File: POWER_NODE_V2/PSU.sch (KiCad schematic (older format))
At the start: 0 parts

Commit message: Schematic for Power Node V2 mostly done - mostly need connectors
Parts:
- added C? (x2): 1uF / 50V / 10% / SMD 0805, symbol C
- added C? (x4): 100n / 50V / 10% / SMD 0603, symbol C
- added C? (x2): 22uF / 16V / 10% / SMD TC3528, symbol CP1
- added C? (x3): 330uF / 35V / 20% / SMD 10x10, symbol CP
- added EL-17-21VGC/TR8 (x3): LED, symbol LED
- added R?: 2.2K / 0.1W / 10% / SMD 0603, symbol R
- added R?: 500 / 0.1W / 10% / SMD 0603, symbol R
- added R?: 300 / 0.1W / 10% / SMD 0603, symbol R
- added U?: R-745.0P, symbol R-745.0P
- added U?: LM1117MP-3.3/NOPB, symbol LM1117MP-3.3/NOPB
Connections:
- net labels added: +24V, +3V3, +5V, GND
- wire segments 0 -> 40
- no-connect marks 0 -> 2
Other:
- note added: "1.5A MAX"
- note added: "4A MAX"
- note added: "Power Supplies"

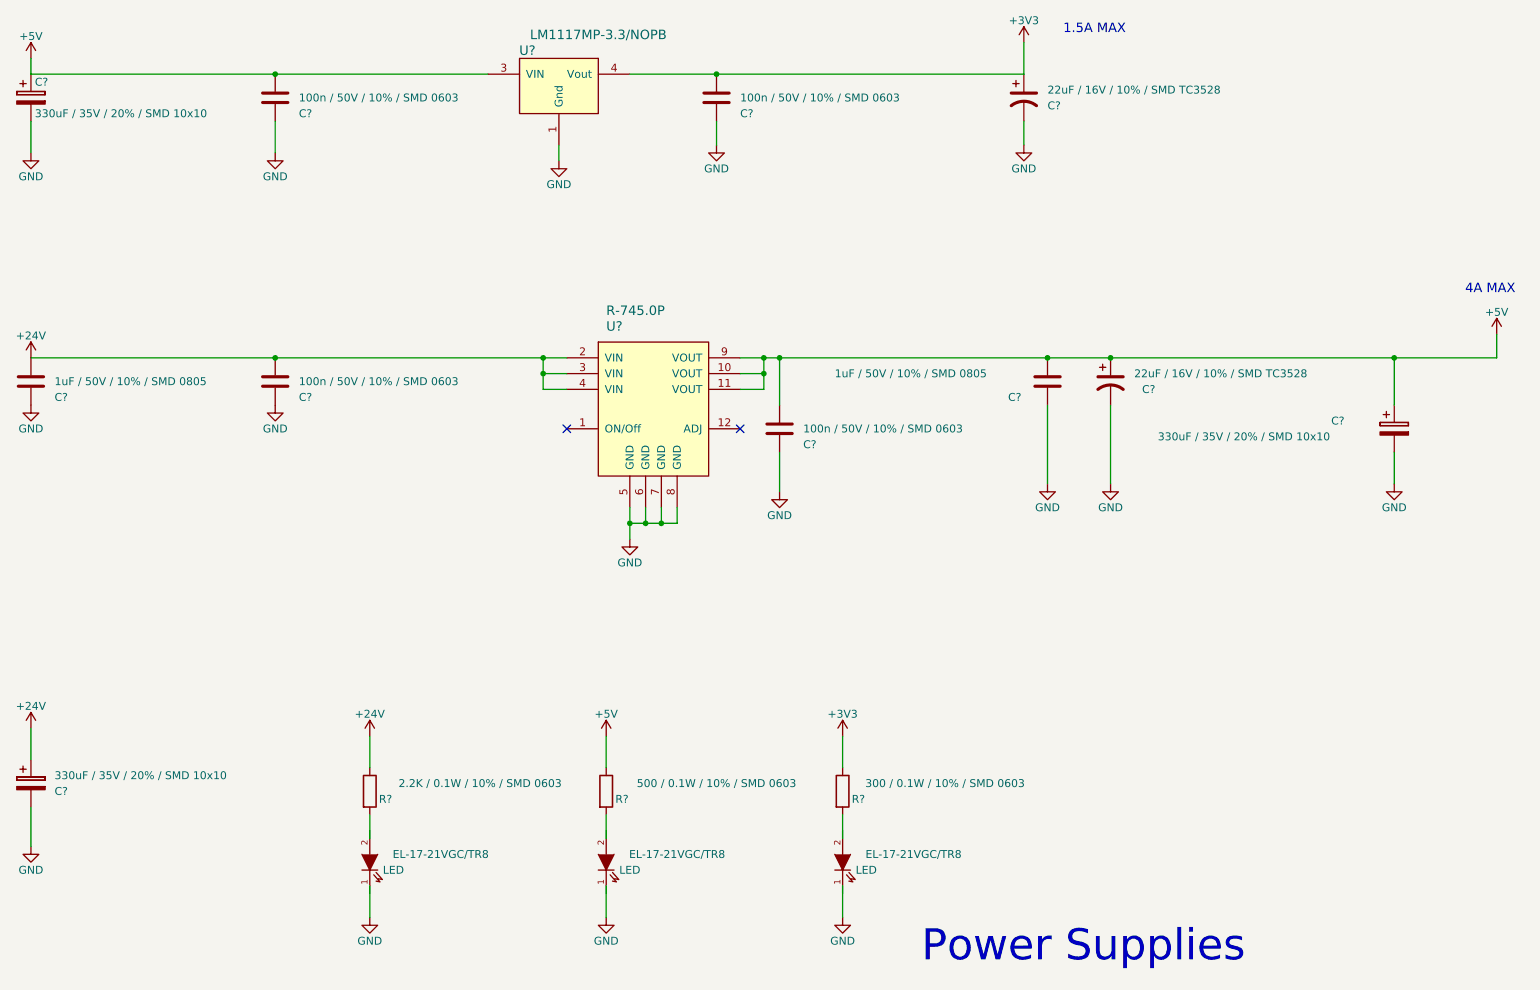
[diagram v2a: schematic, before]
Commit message: made a lot of footprints, began PCB layout for power node v2
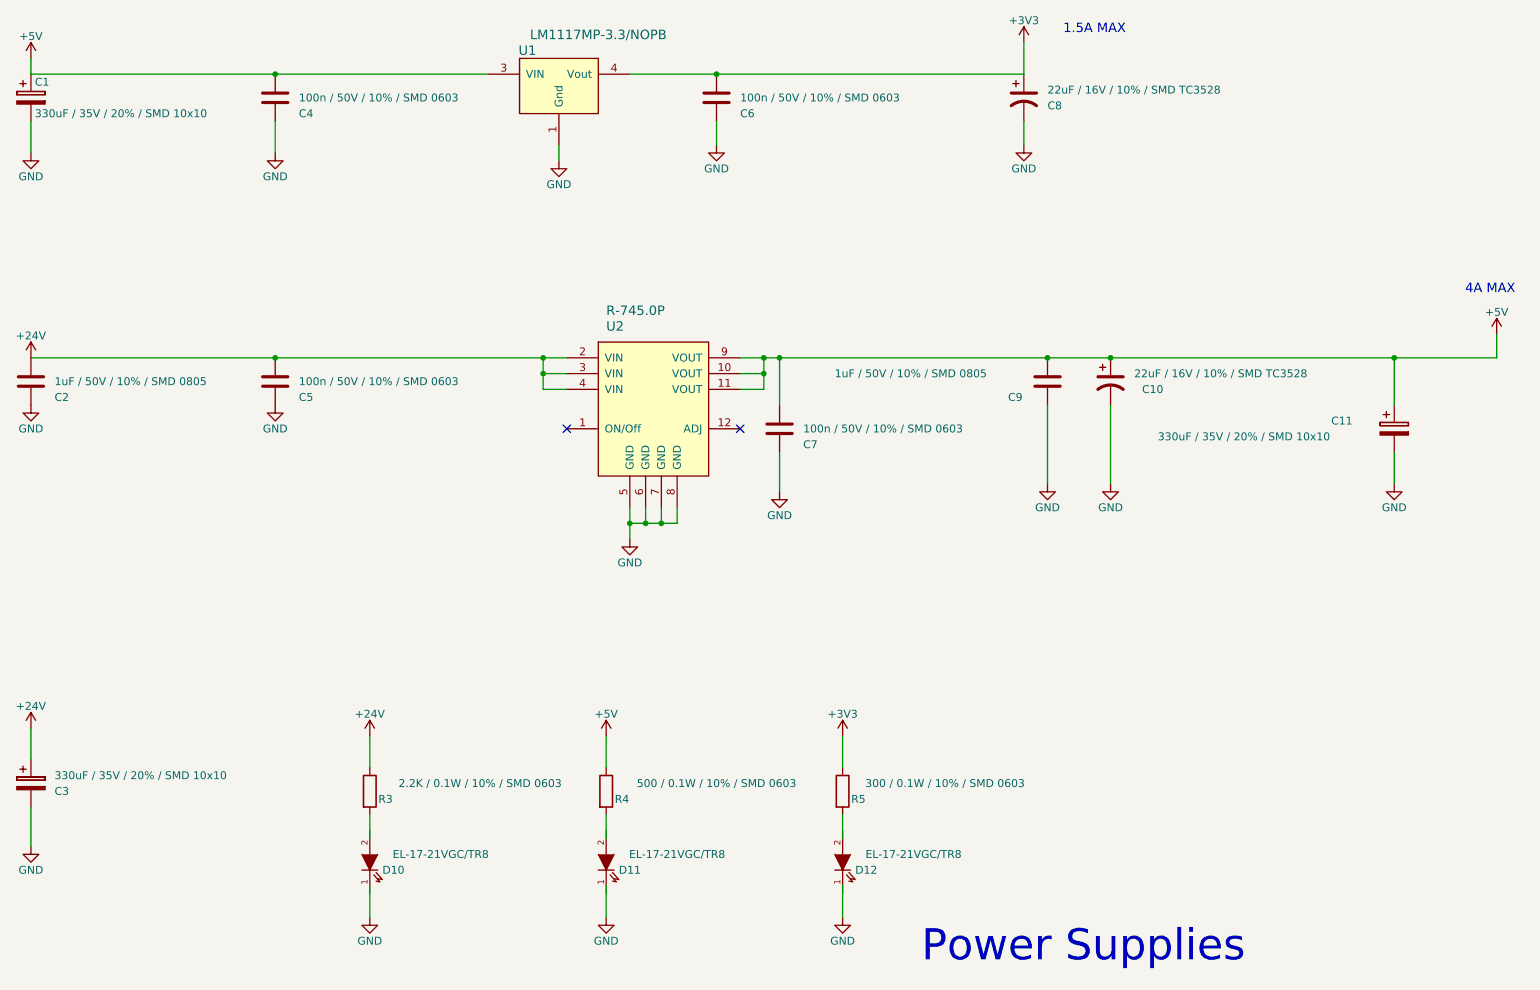
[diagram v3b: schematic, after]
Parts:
- C1, C3: renamed from C?; footprint (none) -> Capacitors_SMD:CP_Elec_10x10
- C10, C8: renamed from C?; footprint (none) -> Capacitors_Tantalum_SMD:CP_Tantalum_Case-T_EIA-3528-12_Reflow
- C11, C4, C5, C6, C7: renamed from C?; footprint (none) -> Capacitors_SMD:C_0603
- C2, C9: renamed from C?; footprint (none) -> Capacitors_SMD:C_0805
- D10, D11, D12: renamed from EL-17-21VGC/TR8; value LED -> EL-17-21VGC/TR8; footprint (none) -> rLoop Footprints:LED_0805
- R3, R4, R5: renamed from R?; footprint (none) -> Resistors_SMD:R_0603
- U1: renamed from U?; footprint (none) -> TO_SOT_Packages_SMD:SOT-223-3Lead_TabPin2
- U2: renamed from U?; footprint (none) -> Socket_Strips:Socket_Strip_Straight_1x12_Pitch2.54mm

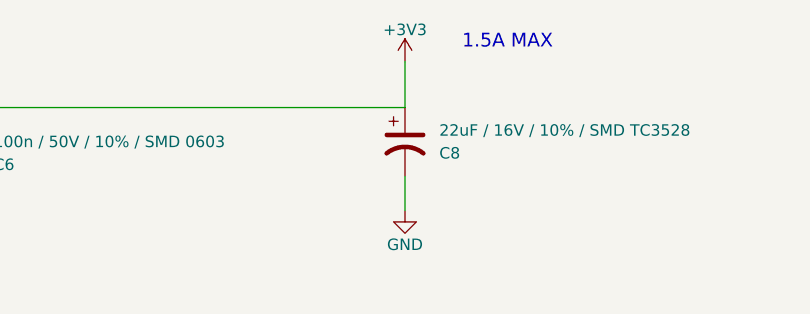
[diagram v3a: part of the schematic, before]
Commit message: Power Node v2 WIP
TODO: 3d models, double check everything, update connector P/N on
schematics, align boards and drill holes
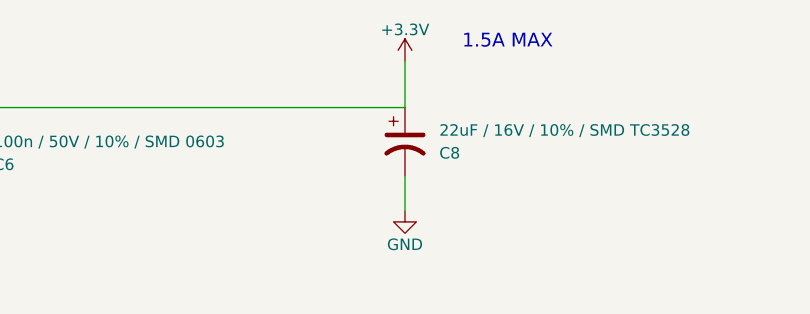
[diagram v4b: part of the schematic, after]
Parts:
- U1: footprint TO_SOT_Packages_SMD:SOT-223-3Lead_TabPin2 -> TO_SOT_Packages_SMD:SOT-223
- U2: footprint Socket_Strips:Socket_Strip_Straight_1x12_Pitch2.54mm -> rLoop Footprints:R-745.0P
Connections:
- net labels added: +3.3V
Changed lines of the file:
@@
 F 0 "U2" H 4500 4200 60  0000 L CNN
 F 1 "R-745.0P" H 4500 4300 60  0000 L CNN
-F 2 "Socket_Strips:Socket_Strip_Straight_1x12_Pitch2.54mm" H 4800 3650 60  0001 C CNN
+F 2 "rLoop Footprints:R-745.0P" H 4800 3650 60  0001 C CNN
 F 3 "" H 4800 3650 60  0001 C CNN
 	1    4800 3650
@@
 F 0 "U1" H 4000 2050 60  0000 C CNN
 F 1 "LM1117MP-3.3/NOPB" H 4450 2150 60  0000 C CNN
-F 2 "TO_SOT_Packages_SMD:SOT-223-3Lead_TabPin2" H 4200 1700 60  0001 C CNN
+F 2 "TO_SOT_Packages_SMD:SOT-223" H 4200 1700 60  0001 C CNN
 F 3 "" H 4200 1700 60  0001 C CNN
 	1    4200 1700
@@
 Wire Wire Line
 	850  1400 850  1500
-$Comp
-L +3V3 #PWR021
-U 1 1 5951E6DF
-P 7150 1300
-F 0 "#PWR021" H 7150 1150 50  0001 C CNN
-F 1 "+3V3" H 7150 1440 50  0000 C CNN
-F 2 "" H 7150 1300 50  0001 C CNN
-F 3 "" H 7150 1300 50  0001 C CNN
-	1    7150 1300
-	1    0    0    -1
-$EndComp
 Wire Wire Line
 	7150 1500 7150 1300
@@
 $EndComp
 $Comp
-L +24V #PWR022
+L +24V #PWR021
 U 1 1 5951E8DB
 P 850 5650
-F 0 "#PWR022" H 850 5500 50  0001 C CNN
+F 0 "#PWR021" H 850 5500 50  0001 C CNN
 F 1 "+24V" H 850 5790 50  0000 C CNN
 F 2 "" H 850 5650 50  0001 C CNN
@@
 	850  5650 850  5850
 $Comp
-L GND #PWR023
+L GND #PWR022
 U 1 1 5951E9DE
 P 850 6400
-F 0 "#PWR023" H 850 6150 50  0001 C CNN
+F 0 "#PWR022" H 850 6150 50  0001 C CNN
 F 1 "GND" H 850 6250 50  0000 C CNN
 F 2 "" H 850 6400 50  0001 C CNN
@@
 	850  6400 850  6150
 $Comp
-L +24V #PWR024
+L +24V #PWR023
 U 1 1 5951EBA8
 P 3000 5700
-F 0 "#PWR024" H 3000 5550 50  0001 C CNN
+F 0 "#PWR023" H 3000 5550 50  0001 C CNN
 F 1 "+24V" H 3000 5840 50  0000 C CNN
 F 2 "" H 3000 5700 50  0001 C CNN
@@
 $EndComp
 $Comp
-L +5V #PWR025
+L +5V #PWR024
 U 1 1 5951EDED
 P 4500 5700
-F 0 "#PWR025" H 4500 5550 50  0001 C CNN
+F 0 "#PWR024" H 4500 5550 50  0001 C CNN
 F 1 "+5V" H 4500 5840 50  0000 C CNN
 F 2 "" H 4500 5700 50  0001 C CNN
@@
 $EndComp
 $Comp
-L +3V3 #PWR026
+L +3V3 #PWR025
 U 1 1 5951EF38
 P 6000 5700
-F 0 "#PWR026" H 6000 5550 50  0001 C CNN
+F 0 "#PWR025" H 6000 5550 50  0001 C CNN
 F 1 "+3V3" H 6000 5840 50  0000 C CNN
 F 2 "" H 6000 5700 50  0001 C CNN
@@
 	6000 6350 6000 6200
 $Comp
-L GND #PWR027
+L GND #PWR026
 U 1 1 5951FDFE
 P 3000 6850
-F 0 "#PWR027" H 3000 6600 50  0001 C CNN
+F 0 "#PWR026" H 3000 6600 50  0001 C CNN
 F 1 "GND" H 3000 6700 50  0000 C CNN
 F 2 "" H 3000 6850 50  0001 C CNN
@@
 $EndComp
 $Comp
-L GND #PWR028
+L GND #PWR027
 U 1 1 5951FE42
 P 4500 6850
-F 0 "#PWR028" H 4500 6600 50  0001 C CNN
+F 0 "#PWR027" H 4500 6600 50  0001 C CNN
 F 1 "GND" H 4500 6700 50  0000 C CNN
 F 2 "" H 4500 6850 50  0001 C CNN
@@
 $EndComp
 $Comp
-L GND #PWR029
+L GND #PWR028
 U 1 1 5951FE86
 P 6000 6850
-F 0 "#PWR029" H 6000 6600 50  0001 C CNN
+F 0 "#PWR028" H 6000 6600 50  0001 C CNN
 F 1 "GND" H 6000 6700 50  0000 C CNN
 F 2 "" H 6000 6850 50  0001 C CNN
@@
 	0    -1   -1   0
 $EndComp
+$Comp
+L +3.3V #PWR029
+U 1 1 5954521C
+P 7150 1300
+F 0 "#PWR029" H 7150 1150 50  0001 C CNN
+F 1 "+3.3V" H 7150 1440 50  0000 C CNN
+F 2 "" H 7150 1300 50  0001 C CNN
+F 3 "" H 7150 1300 50  0001 C CNN
+	1    7150 1300
+	1    0    0    -1
+$EndComp
 $EndSCHEMATC

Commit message: Lot's of progress
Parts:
- removed C11: 330uF / 35V / 20% / SMD 10x10, Capacitors_SMD:C_0603, symbol CP
- D10, D11, D12: footprint rLoop Footprints:LED_0805 -> rLoop_Footprints:LED_0805
- U2: footprint rLoop Footprints:R-745.0P -> rLoop_Footprints:R-745.0P
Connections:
- wire segments 40 -> 38
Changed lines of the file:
@@
 F 0 "U2" H 4500 4200 60  0000 L CNN
 F 1 "R-745.0P" H 4500 4300 60  0000 L CNN
-F 2 "rLoop Footprints:R-745.0P" H 4800 3650 60  0001 C CNN
+F 2 "rLoop_Footprints:R-745.0P" H 4800 3650 60  0001 C CNN
 F 3 "" H 4800 3650 60  0001 C CNN
 	1    4800 3650
@@
 Connection ~ 4100 3400
 Wire Wire Line
-	5350 3300 10150 3300
+	5350 3300 9050 3300
 Connection ~ 7300 3300
-Wire Wire Line
-	9500 3300 9500 3600
 Connection ~ 7700 3300
-Wire Wire Line
-	10150 3300 10150 3150
-Connection ~ 9500 3300
 $Comp
 L +5V #PWR09
 U 1 1 5951D667
-P 10150 3150
-F 0 "#PWR09" H 10150 3000 50  0001 C CNN
-F 1 "+5V" H 10150 3290 50  0000 C CNN
-F 2 "" H 10150 3150 50  0001 C CNN
-F 3 "" H 10150 3150 50  0001 C CNN
-	1    10150 3150
+P 9050 3100
+F 0 "#PWR09" H 9050 2950 50  0001 C CNN
+F 1 "+5V" H 9050 3240 50  0000 C CNN
+F 2 "" H 9050 3100 50  0001 C CNN
+F 3 "" H 9050 3100 50  0001 C CNN
+	1    9050 3100
 	1    0    0    -1
 $EndComp
@@
 	1    0    0    -1
 $EndComp
-$Comp
-L GND #PWR014
-U 1 1 5951D930
-P 9500 4100
-F 0 "#PWR014" H 9500 3850 50  0001 C CNN
-F 1 "GND" H 9500 3950 50  0000 C CNN
-F 2 "" H 9500 4100 50  0001 C CNN
-F 3 "" H 9500 4100 50  0001 C CNN
-	1    9500 4100
-	1    0    0    -1
-$EndComp
-Wire Wire Line
-	9500 4100 9500 3900
 Wire Wire Line
 	7700 3600 7700 4100
@@
 $EndComp
 $Comp
-L CP C11
-U 1 1 5951DE4C
-P 9500 3750
-F 0 "C11" H 9100 3800 50  0000 L CNN
-F 1 "330uF / 35V / 20% / SMD 10x10" H 8000 3700 50  0000 L CNN
-F 2 "Capacitors_SMD:C_0603" H 9538 3600 50  0001 C CNN
-F 3 "" H 9500 3750 50  0001 C CNN
-	1    9500 3750
-	1    0    0    -1
-$EndComp
-$Comp
 L CP C1
 U 1 1 5951DF24
@@
 Text Notes 7400 1250 0    60   ~ 0
 1.5A MAX
-Text Notes 9950 2900 0    60   ~ 0
+Text Notes 8950 2900 0    60   ~ 0
 4A MAX
 Text Notes 6500 7150 0    197  ~ 0
@@
 F 0 "D12" V 5950 6350 50  0000 C CNN
 F 1 "EL-17-21VGC/TR8" V 6050 6050 50  0000 C CNN
-F 2 "rLoop Footprints:LED_0805" H 6000 6500 50  0001 C CNN
+F 2 "rLoop_Footprints:LED_0805" H 6000 6500 50  0001 C CNN
 F 3 "" H 6000 6500 50  0001 C CNN
 	1    6000 6500
@@
 F 0 "D11" V 4450 6350 50  0000 C CNN
 F 1 "EL-17-21VGC/TR8" V 4550 6050 50  0000 C CNN
-F 2 "rLoop Footprints:LED_0805" H 4500 6500 50  0001 C CNN
+F 2 "rLoop_Footprints:LED_0805" H 4500 6500 50  0001 C CNN
 F 3 "" H 4500 6500 50  0001 C CNN
 	1    4500 6500
@@
 F 0 "D10" V 2950 6350 50  0000 C CNN
 F 1 "EL-17-21VGC/TR8" V 3050 6050 50  0000 C CNN
-F 2 "rLoop Footprints:LED_0805" H 3000 6500 50  0001 C CNN
+F 2 "rLoop_Footprints:LED_0805" H 3000 6500 50  0001 C CNN
 F 3 "" H 3000 6500 50  0001 C CNN
 	1    3000 6500
@@
 	1    0    0    -1
 $EndComp
+Wire Wire Line
+	9050 3300 9050 3100
 $EndSCHEMATC

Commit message: Added tooling holes & fiducial marks
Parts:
- D10, D11, D12: symbol LED -> LED-RESCUE-POWER_NODE_V2
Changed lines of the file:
@@
 EESchema Schematic File Version 2
+LIBS:POWER_NODE_V2-rescue
 LIBS:power
 LIBS:device
@@
 $Descr USLetter 11000 8500
 encoding utf-8
-Sheet 3 9
+Sheet 3 10
 Title ""
 Date ""
@@
 $EndComp
 $Comp
-L +24V #PWR06
+L +24V #PWR8
 U 1 1 5951CE6E
 P 850 3300
-F 0 "#PWR06" H 850 3150 50  0001 C CNN
+F 0 "#PWR8" H 850 3150 50  0001 C CNN
 F 1 "+24V" H 850 3440 50  0000 C CNN
 F 2 "" H 850 3300 50  0001 C CNN
@@
 $EndComp
 $Comp
-L GND #PWR07
+L GND #PWR9
 U 1 1 5951CF02
 P 850 3600
-F 0 "#PWR07" H 850 3350 50  0001 C CNN
+F 0 "#PWR9" H 850 3350 50  0001 C CNN
 F 1 "GND" H 850 3450 50  0000 C CNN
 F 2 "" H 850 3600 50  0001 C CNN
@@
 $EndComp
 $Comp
-L GND #PWR08
+L GND #PWR13
 U 1 1 5951D0AA
 P 2400 3600
-F 0 "#PWR08" H 2400 3350 50  0001 C CNN
+F 0 "#PWR13" H 2400 3350 50  0001 C CNN
 F 1 "GND" H 2400 3450 50  0000 C CNN
 F 2 "" H 2400 3600 50  0001 C CNN
@@
 Connection ~ 7700 3300
 $Comp
-L +5V #PWR09
+L +5V #PWR28
 U 1 1 5951D667
 P 9050 3100
-F 0 "#PWR09" H 9050 2950 50  0001 C CNN
+F 0 "#PWR28" H 9050 2950 50  0001 C CNN
 F 1 "+5V" H 9050 3240 50  0000 C CNN
 F 2 "" H 9050 3100 50  0001 C CNN
@@
 Connection ~ 5500 3400
 $Comp
-L GND #PWR010
+L GND #PWR19
 U 1 1 5951D759
 P 4650 4450
-F 0 "#PWR010" H 4650 4200 50  0001 C CNN
+F 0 "#PWR19" H 4650 4200 50  0001 C CNN
 F 1 "GND" H 4650 4300 50  0000 C CNN
 F 2 "" H 4650 4450 50  0001 C CNN
@@
 Connection ~ 4850 4350
 $Comp
-L GND #PWR011
+L GND #PWR21
 U 1 1 5951D8AB
 P 5600 4150
-F 0 "#PWR011" H 5600 3900 50  0001 C CNN
+F 0 "#PWR21" H 5600 3900 50  0001 C CNN
 F 1 "GND" H 5600 4000 50  0000 C CNN
 F 2 "" H 5600 4150 50  0001 C CNN
@@
 	5600 4150 5600 3900
 $Comp
-L GND #PWR012
+L GND #PWR26
 U 1 1 5951D8F0
 P 7300 4100
-F 0 "#PWR012" H 7300 3850 50  0001 C CNN
+F 0 "#PWR26" H 7300 3850 50  0001 C CNN
 F 1 "GND" H 7300 3950 50  0000 C CNN
 F 2 "" H 7300 4100 50  0001 C CNN
@@
 $EndComp
 $Comp
-L GND #PWR013
+L GND #PWR27
 U 1 1 5951D910
 P 7700 4100
-F 0 "#PWR013" H 7700 3850 50  0001 C CNN
+F 0 "#PWR27" H 7700 3850 50  0001 C CNN
 F 1 "GND" H 7700 3950 50  0000 C CNN
 F 2 "" H 7700 4100 50  0001 C CNN
@@
 $EndComp
 $Comp
-L GND #PWR014
+L GND #PWR12
 U 1 1 5951E398
 P 2400 2000
-F 0 "#PWR014" H 2400 1750 50  0001 C CNN
+F 0 "#PWR12" H 2400 1750 50  0001 C CNN
 F 1 "GND" H 2400 1850 50  0000 C CNN
 F 2 "" H 2400 2000 50  0001 C CNN
@@
 	2400 2000 2400 1800
 $Comp
-L GND #PWR015
+L GND #PWR7
 U 1 1 5951E401
 P 850 2000
-F 0 "#PWR015" H 850 1750 50  0001 C CNN
+F 0 "#PWR7" H 850 1750 50  0001 C CNN
 F 1 "GND" H 850 1850 50  0000 C CNN
 F 2 "" H 850 2000 50  0001 C CNN
@@
 $EndComp
 $Comp
-L GND #PWR016
+L GND #PWR20
 U 1 1 5951E430
 P 5200 1950
-F 0 "#PWR016" H 5200 1700 50  0001 C CNN
+F 0 "#PWR20" H 5200 1700 50  0001 C CNN
 F 1 "GND" H 5200 1800 50  0000 C CNN
 F 2 "" H 5200 1950 50  0001 C CNN
@@
 $EndComp
 $Comp
-L GND #PWR017
+L GND #PWR25
 U 1 1 5951E45F
 P 7150 1950
-F 0 "#PWR017" H 7150 1700 50  0001 C CNN
+F 0 "#PWR25" H 7150 1700 50  0001 C CNN
 F 1 "GND" H 7150 1800 50  0000 C CNN
 F 2 "" H 7150 1950 50  0001 C CNN
@@
 	5200 1950 5200 1800
 $Comp
-L GND #PWR018
+L GND #PWR16
 U 1 1 5951E4ED
 P 4200 2050
-F 0 "#PWR018" H 4200 1800 50  0001 C CNN
+F 0 "#PWR16" H 4200 1800 50  0001 C CNN
 F 1 "GND" H 4200 1900 50  0000 C CNN
 F 2 "" H 4200 2050 50  0001 C CNN
@@
 Connection ~ 5200 1500
 $Comp
-L +5V #PWR019
+L +5V #PWR6
 U 1 1 5951E683
 P 850 1400
-F 0 "#PWR019" H 850 1250 50  0001 C CNN
+F 0 "#PWR6" H 850 1250 50  0001 C CNN
 F 1 "+5V" H 850 1540 50  0000 C CNN
 F 2 "" H 850 1400 50  0001 C CNN
@@
 $EndComp
 $Comp
-L +24V #PWR020
+L +24V #PWR10
 U 1 1 5951E8DB
 P 850 5650
-F 0 "#PWR020" H 850 5500 50  0001 C CNN
+F 0 "#PWR10" H 850 5500 50  0001 C CNN
 F 1 "+24V" H 850 5790 50  0000 C CNN
 F 2 "" H 850 5650 50  0001 C CNN
@@
 	850  5650 850  5850
 $Comp
-L GND #PWR021
+L GND #PWR11
 U 1 1 5951E9DE
 P 850 6400
-F 0 "#PWR021" H 850 6150 50  0001 C CNN
+F 0 "#PWR11" H 850 6150 50  0001 C CNN
 F 1 "GND" H 850 6250 50  0000 C CNN
 F 2 "" H 850 6400 50  0001 C CNN
@@
 	850  6400 850  6150
 $Comp
-L +24V #PWR022
+L +24V #PWR14
 U 1 1 5951EBA8
 P 3000 5700
-F 0 "#PWR022" H 3000 5550 50  0001 C CNN
+F 0 "#PWR14" H 3000 5550 50  0001 C CNN
 F 1 "+24V" H 3000 5840 50  0000 C CNN
 F 2 "" H 3000 5700 50  0001 C CNN
@@
 $EndComp
 $Comp
-L +5V #PWR023
+L +5V #PWR17
 U 1 1 5951EDED
 P 4500 5700
-F 0 "#PWR023" H 4500 5550 50  0001 C CNN
+F 0 "#PWR17" H 4500 5550 50  0001 C CNN
 F 1 "+5V" H 4500 5840 50  0000 C CNN
 F 2 "" H 4500 5700 50  0001 C CNN
@@
 $EndComp
 $Comp
-L +3V3 #PWR024
+L +3V3 #PWR22
 U 1 1 5951EF38
 P 6000 5700
-F 0 "#PWR024" H 6000 5550 50  0001 C CNN
+F 0 "#PWR22" H 6000 5550 50  0001 C CNN
 F 1 "+3V3" H 6000 5840 50  0000 C CNN
 F 2 "" H 6000 5700 50  0001 C CNN
@@
 	6000 6350 6000 6200
 $Comp
-L GND #PWR025
+L GND #PWR15
 U 1 1 5951FDFE
 P 3000 6850
-F 0 "#PWR025" H 3000 6600 50  0001 C CNN
+F 0 "#PWR15" H 3000 6600 50  0001 C CNN
 F 1 "GND" H 3000 6700 50  0000 C CNN
 F 2 "" H 3000 6850 50  0001 C CNN
@@
 $EndComp
 $Comp
-L GND #PWR026
+L GND #PWR18
 U 1 1 5951FE42
 P 4500 6850
-F 0 "#PWR026" H 4500 6600 50  0001 C CNN
+F 0 "#PWR18" H 4500 6600 50  0001 C CNN
 F 1 "GND" H 4500 6700 50  0000 C CNN
 F 2 "" H 4500 6850 50  0001 C CNN
@@
 $EndComp
 $Comp
-L GND #PWR027
+L GND #PWR23
 U 1 1 5951FE86
 P 6000 6850
-F 0 "#PWR027" H 6000 6600 50  0001 C CNN
+F 0 "#PWR23" H 6000 6600 50  0001 C CNN
 F 1 "GND" H 6000 6700 50  0000 C CNN
 F 2 "" H 6000 6850 50  0001 C CNN
@@
 Power Supplies
 $Comp
-L LED D12
+L LED-RESCUE-POWER_NODE_V2 D12
 U 1 1 5951EBFD
 P 6000 6500
@@
 $EndComp
 $Comp
-L LED D11
+L LED-RESCUE-POWER_NODE_V2 D11
 U 1 1 5951EB65
 P 4500 6500
@@
 $EndComp
 $Comp
-L LED D10
+L LED-RESCUE-POWER_NODE_V2 D10
 U 1 1 5951EAEA
 P 3000 6500
@@
 $EndComp
 $Comp
-L +3.3V #PWR028
+L +3.3V #PWR24
 U 1 1 5954521C
 P 7150 1300
-F 0 "#PWR028" H 7150 1150 50  0001 C CNN
+F 0 "#PWR24" H 7150 1150 50  0001 C CNN
 F 1 "+3.3V" H 7150 1440 50  0000 C CNN
 F 2 "" H 7150 1300 50  0001 C CNN
